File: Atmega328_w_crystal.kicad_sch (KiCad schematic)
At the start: 6 parts, among them U1401 HEADER_3x2, U1402 ATmega328-A, Y1401 crystal_arduino

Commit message: made additions to the project
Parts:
- added R1: 10k, Resistor_SMD:R_1206_3216Metric_Pad1.30x1.75mm_HandSolder, symbol Device:R
- added SW1: SW_SPST, Button_Switch_SMD:SW_SPST_SKQG_WithStem, symbol Switch:SW_SPST
- R1401: value R -> 10k
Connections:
- net +5V: now also R1.1
- net GND: now also SW1.1 (A)
- net at U1402.22 (ADC7): now also R1.2, SW1.2 (B)
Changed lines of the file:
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@@
   (junction (at 64.77 87.63) (diameter 0) (color 0 0 0 0)
   )
+  (junction (at 62.23 63.5) (diameter 0) (color 0 0 0 0)
+  )
   (wire (pts (xy 48.895 84.455) (xy 48.895 91.44))
     (stroke (width 0) (type default) (color 0 0 0 0))
@@
     (stroke (width 0) (type default) (color 0 0 0 0))
   )
+  (wire (pts (xy 62.23 54.61) (xy 62.23 55.88))
+    (stroke (width 0) (type default) (color 0 0 0 0))
+  )
+  (wire (pts (xy 45.72 63.5) (xy 49.53 63.5))
+    (stroke (width 0) (type default) (color 0 0 0 0))
+  )
   (wire (pts (xy 105.41 73.66) (xy 107.95 73.66))
     (stroke (width 0) (type default) (color 0 0 0 0))
@@
   )
   (wire (pts (xy 34.925 113.03) (xy 34.925 114.3))
+    (stroke (width 0) (type default) (color 0 0 0 0))
+  )
+  (wire (pts (xy 62.23 63.5) (xy 74.93 63.5))
+    (stroke (width 0) (type default) (color 0 0 0 0))
+  )
+  (wire (pts (xy 59.69 63.5) (xy 62.23 63.5))
     (stroke (width 0) (type default) (color 0 0 0 0))
   )
@@
     )
     (property "Datasheet" "" (id 3) (at 64.77 100.33 0)
+      (effects (font (size 1.27 1.27)) hide)
+    )
+    (pin "1")
+  )
+  (symbol (lib_id "power:GND") (at 45.72 63.5 0) (unit 1)
+    (in_bom yes) (on_board yes) (fields_autoplaced)
+    (property "Reference" "#PWR0101" (id 0) (at 45.72 69.85 0)
+      (effects (font (size 1.27 1.27)) hide)
+    )
+    (property "Value" "GND" (id 1) (at 45.72 67.9434 0))
+    (property "Footprint" "" (id 2) (at 45.72 63.5 0)
+      (effects (font (size 1.27 1.27)) hide)
+    )
+    (property "Datasheet" "" (id 3) (at 45.72 63.5 0)
       (effects (font (size 1.27 1.27)) hide)
     )
@@
     (pin "1")
   )
+  (symbol (lib_id "Switch:SW_SPST") (at 54.61 63.5 0) (unit 1)
+    (in_bom yes) (on_board yes) (fields_autoplaced)
+    (property "Reference" "SW1" (id 0) (at 54.61 58.1492 0))
+    (property "Value" "SW_SPST" (id 1) (at 54.61 60.6861 0))
+    (property "Footprint" "Button_Switch_SMD:SW_SPST_SKQG_WithStem" (id 2) (at 54.61 63.5 0)
+      (effects (font (size 1.27 1.27)) hide)
+    )
+    (property "Datasheet" "~" (id 3) (at 54.61 63.5 0)
+      (effects (font (size 1.27 1.27)) hide)
+    )
+    (property "JLCPCB Part#" "C318884" (id 4) (at 54.61 63.5 0)
+      (effects (font (size 1.27 1.27)) hide)
+    )
+    (pin "1")
+    (pin "2")
+  )
   (symbol (lib_id "power:GND") (at 69.85 83.185 0) (unit 1)
     (in_bom yes) (on_board yes) (fields_autoplaced)
@@
     )
     (pin "1")
+  )
+  (symbol (lib_id "Device:R") (at 62.23 59.69 0) (unit 1)
+    (in_bom yes) (on_board yes) (fields_autoplaced)
+    (property "Reference" "R1" (id 0) (at 64.008 58.8553 0)
+      (effects (font (size 1.27 1.27)) (justify left))
+    )
+    (property "Value" "10k" (id 1) (at 64.008 61.3922 0)
+      (effects (font (size 1.27 1.27)) (justify left))
+    )
+    (property "Footprint" "Resistor_SMD:R_1206_3216Metric_Pad1.30x1.75mm_HandSolder" (id 2) (at 60.452 59.69 90)
+      (effects (font (size 1.27 1.27)) hide)
+    )
+    (property "Datasheet" "~" (id 3) (at 62.23 59.69 0)
+      (effects (font (size 1.27 1.27)) hide)
+    )
+    (property "JLCPCB Part#" "C17902" (id 4) (at 62.23 59.69 0)
+      (effects (font (size 1.27 1.27)) hide)
+    )
+    (pin "1")
+    (pin "2")
   )
   (symbol (lib_id "power:+5V") (at 90.17 45.72 0) (unit 1)
@@
     (pin "6")
   )
+  (symbol (lib_id "power:+5V") (at 62.23 54.61 0) (unit 1)
+    (in_bom yes) (on_board yes) (fields_autoplaced)
+    (property "Reference" "#PWR0102" (id 0) (at 62.23 58.42 0)
+      (effects (font (size 1.27 1.27)) hide)
+    )
+    (property "Value" "+5V" (id 1) (at 62.23 51.0342 0))
+    (property "Footprint" "" (id 2) (at 62.23 54.61 0)
+      (effects (font (size 1.27 1.27)) hide)
+    )
+    (property "Datasheet" "" (id 3) (at 62.23 54.61 0)
+      (effects (font (size 1.27 1.27)) hide)
+    )
+    (pin "1")
+  )
   (symbol (lib_id "power:GND") (at 62.865 121.92 0) (unit 1)
     (in_bom yes) (on_board yes)
@@
       (effects (font (size 1.27 1.27)) (justify left))
     )
-    (property "Value" "R" (id 1) (at 36.703 119.8122 0)
-      (effects (font (size 1.27 1.27)) (justify left))
-    )
+    (property "Value" "10k" (id 1) (at 36.703 119.8122 0)
+      (effects (font (size 1.27 1.27)) (justify left))
+    )

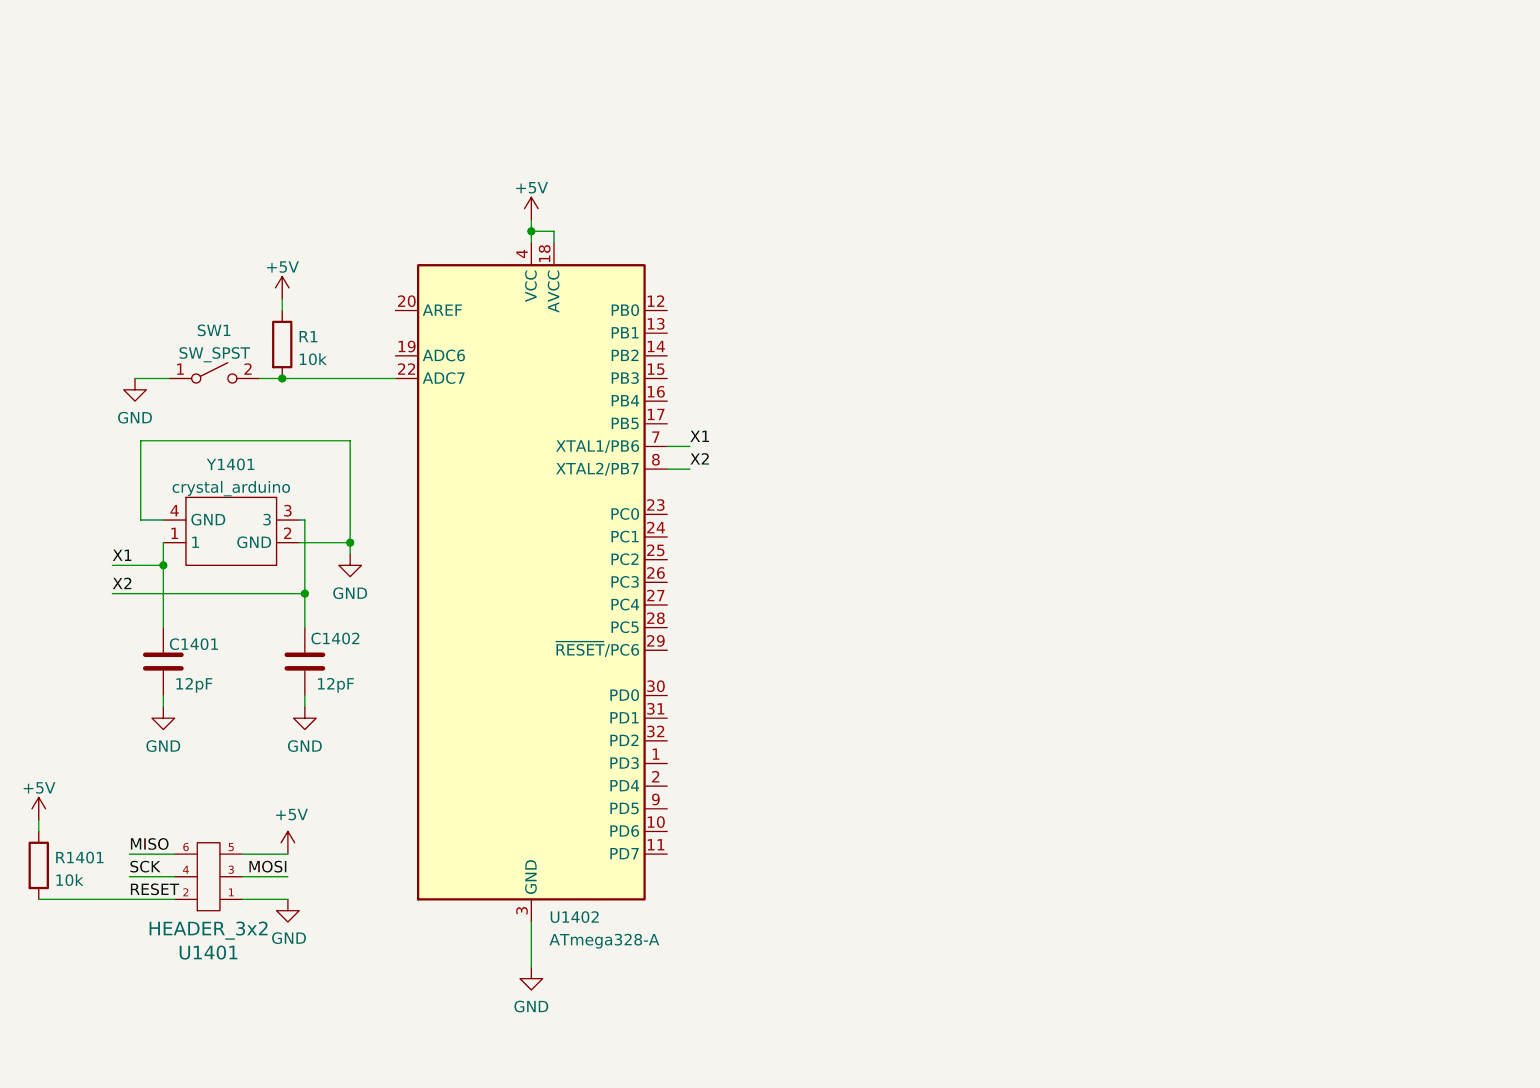
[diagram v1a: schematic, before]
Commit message: added ch340.sch
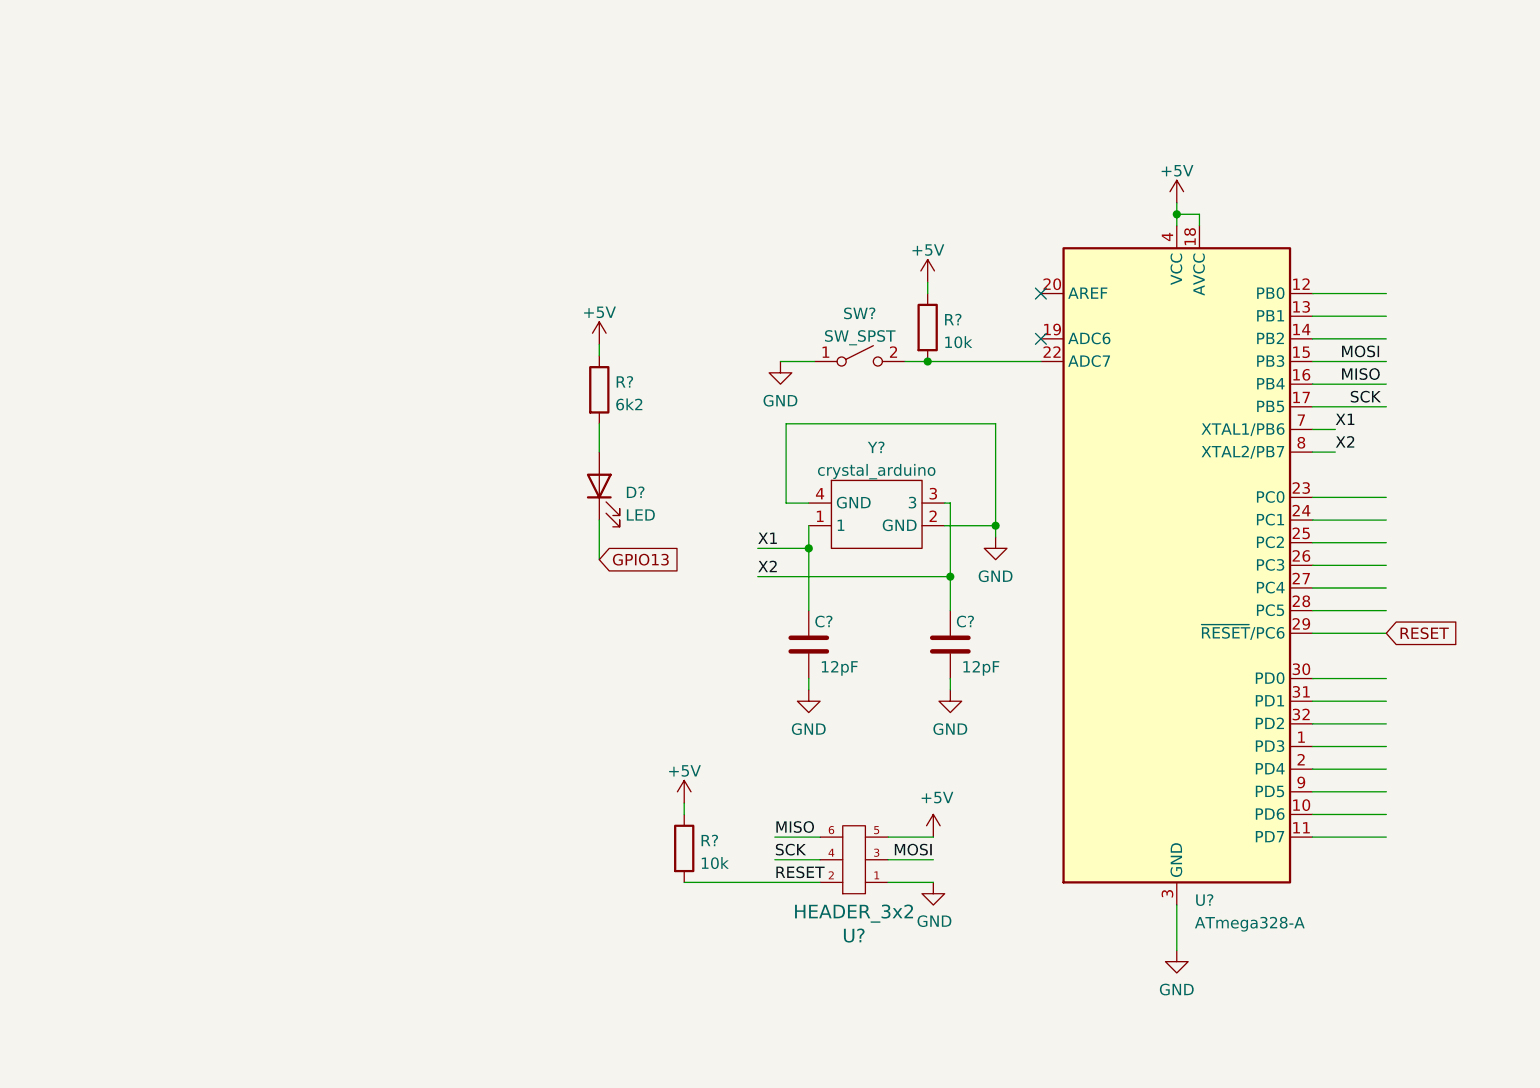
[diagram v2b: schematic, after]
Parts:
- removed C1401, C1402: 12pF, Capacitor_SMD:C_0805_2012Metric_Pad1.18x1.45mm_HandSolder, symbol Device:C
- removed R1, R1401: 10k, Resistor_SMD:R_1206_3216Metric_Pad1.30x1.75mm_HandSolder, symbol Device:R
- removed SW1: SW_SPST, Button_Switch_SMD:SW_SPST_SKQG_WithStem, symbol Switch:SW_SPST
- removed U1401: HEADER_3x2, Connector_PinSocket_1.27mm:PinSocket_2x03_P1.27mm_Vertical, symbol servoDriverSMD-rescue:HEADER_3x2-w_connectors
- removed U1402: ATmega328-A, Package_QFP:TQFP-32_7x7mm_P0.8mm, symbol MCU_Microchip_ATmega:ATmega328-A
- removed Y1401: crystal_arduino, custom_kicad_lib_sk:crystal_arduino, symbol custom_bas:crystal_arduino
- added C? (x2): 12pF, Capacitor_SMD:C_0402_1005Metric_Pad0.74x0.62mm_HandSolder, symbol Device:C
- added D?: LED, LED_SMD:LED_0805_2012Metric_Pad1.15x1.40mm_HandSolder, symbol Device:LED
- added R?: 6k2, Resistor_SMD:R_0603_1608Metric_Pad0.98x0.95mm_HandSolder, symbol Device:R
- added R? (x2): 10k, Resistor_SMD:R_0402_1005Metric_Pad0.72x0.64mm_HandSolder, symbol Device:R
- added SW?: SW_SPST, Button_Switch_SMD:SW_SPST_SKQG_WithStem, symbol Switch:SW_SPST
- added U?: ATmega328-A, Package_QFP:TQFP-32_7x7mm_P0.8mm, symbol MCU_Microchip_ATmega:ATmega328-A
- added U?: HEADER_3x2, Connector_PinSocket_1.27mm:PinSocket_2x03_P1.27mm_Vertical, symbol servoDriverSMD-rescue:HEADER_3x2-w_connectors
- added Y?: crystal_arduino, custom_kicad_lib_sk:crystal_arduino, symbol custom_bas:crystal_arduino
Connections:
- net +5V: now also R?.1, R?.1, R?.1, U?.18 (AVCC), U?.4 (VCC), U?.5, U?.6 (VCC)
- net GND: now also C?.1, C?.1, SW?.1 (A), U?.1, U?.21 (GND), U?.3 (GND), U?.5 (GND), Y?.2 (GND), Y?.4 (GND)
- net MISO: now also U?.16 (PB4), U?.6
- net MOSI: now also U?.15 (PB3), U?.3
- net RESET: now also R?.2, U?.2, U?.29 (~{RESET}/PC6)
- net SCK: now also U?.17 (PB5), U?.4
- net X1: now also C?.2, U?.7 (XTAL1/PB6), Y?.1
- net X2: now also C?.2, U?.8 (XTAL2/PB7), Y?.3
- new net: D?.2 (A), R?.2
- new net: R?.2, SW?.2 (B), U?.22 (ADC7)
- new net GPIO13: D?.1 (K)
- no-connect marks 0 -> 2

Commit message: added decoupling capacitor to atmega schematic
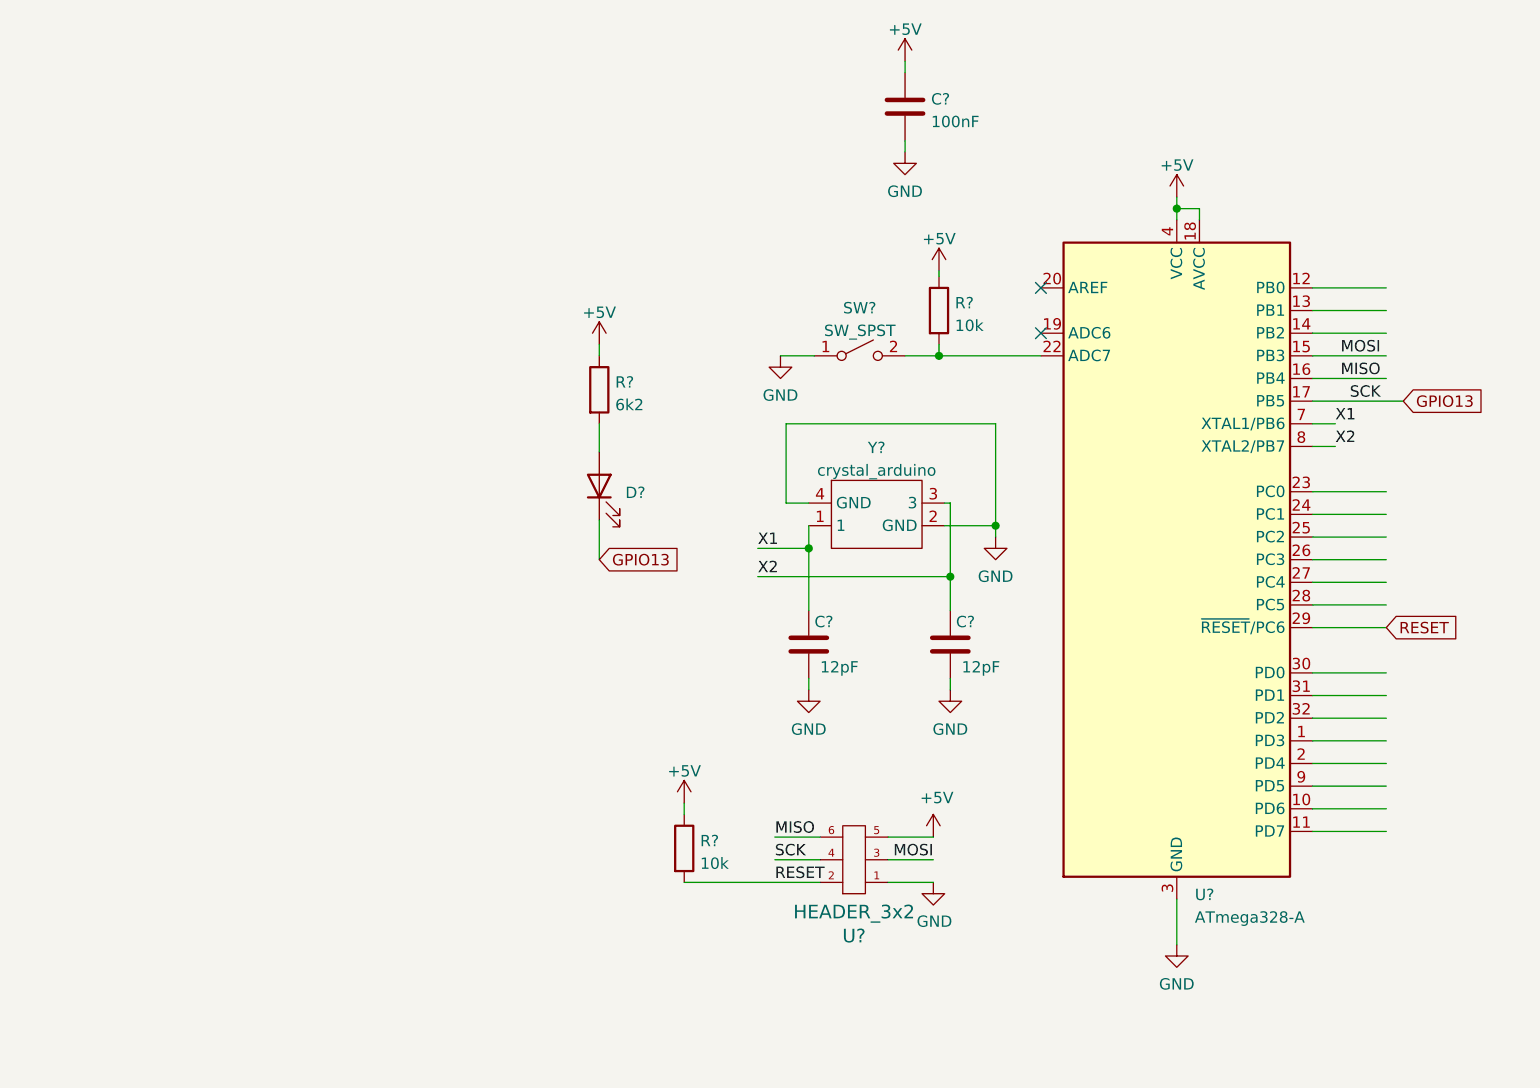
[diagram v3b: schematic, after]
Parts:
- added C?: 100nF, Capacitor_SMD:C_0603_1608Metric_Pad1.08x0.95mm_HandSolder, symbol Device:C
- D?: value LED -> (none); footprint LED_SMD:LED_0805_2012Metric_Pad1.15x1.40mm_HandSolder -> (none); JLCPCB Part# (none) -> C84256
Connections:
- net SCK is gone; now on net GPIO13: U?.17 (PB5), U?.4
- net +5V: now also C?.2
- net GND: now also C?.1
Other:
- moved on the sheet: R?, SW?, U?

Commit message: minor update with partnumbers and footprints
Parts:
- D?: value (none) -> LED; footprint (none) -> LED_SMD:LED_0805_2012Metric_Pad1.15x1.40mm_HandSolder
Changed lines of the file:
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@@
       (effects (font (size 1.27 1.27)) (justify right))
     )
-    (property "Value" "" (id 1) (at 100.711 78.8547 90)
+    (property "Value" "LED" (id 1) (at 100.711 78.8547 90)
       (effects (font (size 1.27 1.27)) (justify right))
     )
-    (property "Footprint" "" (id 2) (at 97.79 75.565 0)
+    (property "Footprint" "LED_SMD:LED_0805_2012Metric_Pad1.15x1.40mm_HandSolder" (id 2) (at 97.79 75.565 0)
       (effects (font (size 1.27 1.27)) hide)
     )
